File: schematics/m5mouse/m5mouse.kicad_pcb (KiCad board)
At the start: 2 copper layers, 103 x 50 mm, 98 parts, among them IC1 LM3940IMP-3.3_NOPB, J1 Conn_01x02, J2 M-BUS, J3 SWD, J4 Conn_02x03_Odd_Even, J5 Conn_02x03_Odd_Even, J6 Conn_01x03, J7 Conn_01x06, J8 Conn_01x06, Q1 BSS138, Q2 ST-1KL3A, Q3 BSS138, Q4 ST-1KL3A, Q5 BSS138, Q6 ST-1KL3A, Q7 BSS138, Q8 ST-1KL3A, SW1 SW_SPDT, SW2 SW_Push, U1 TPS562200, U2 STM32F405RGTx, U3 DRV8835, U4 ICM-20648, Y1 8MHz, Y2 32.768kHz

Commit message: Fix path
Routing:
- net +3V3: track 203.6 -> 199.1 mm, vias 5 -> 6
- net Net-(C19-Pad1): track 65.8 -> 64.9 mm

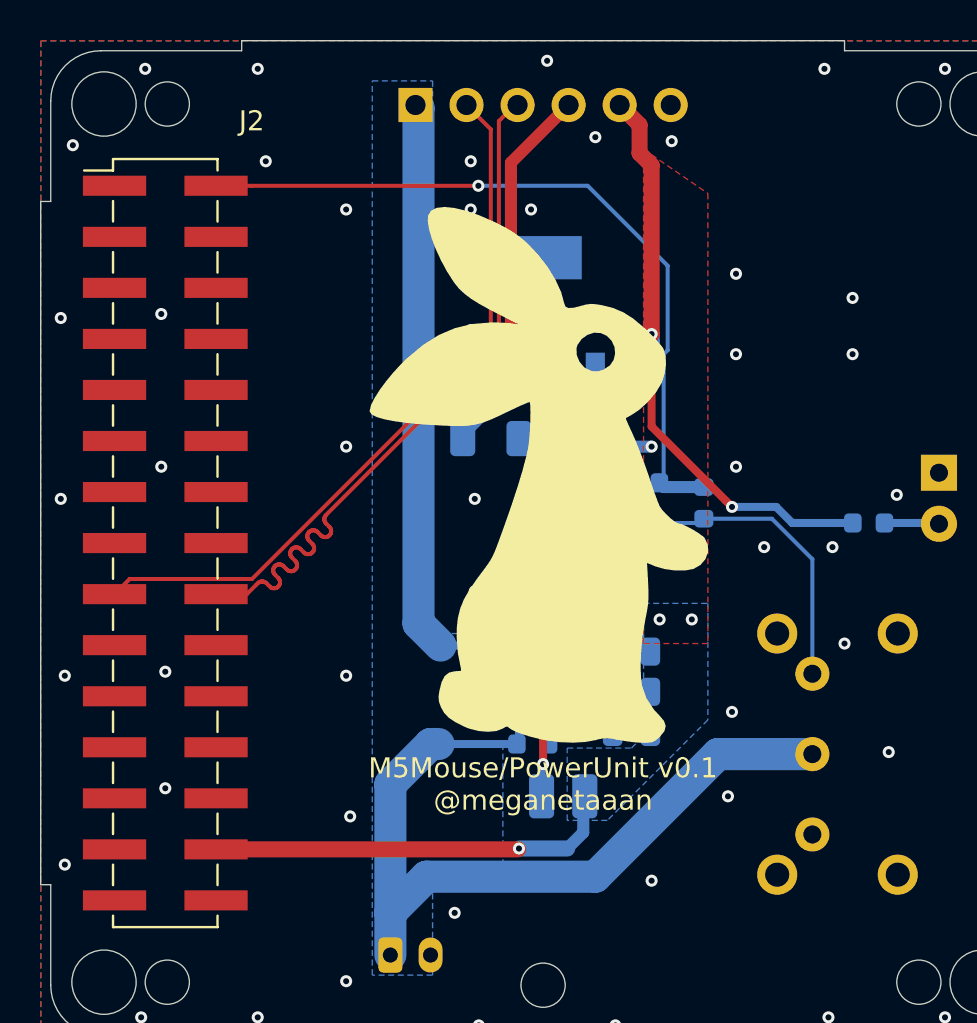
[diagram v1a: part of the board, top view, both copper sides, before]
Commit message: Fix flipped pin header
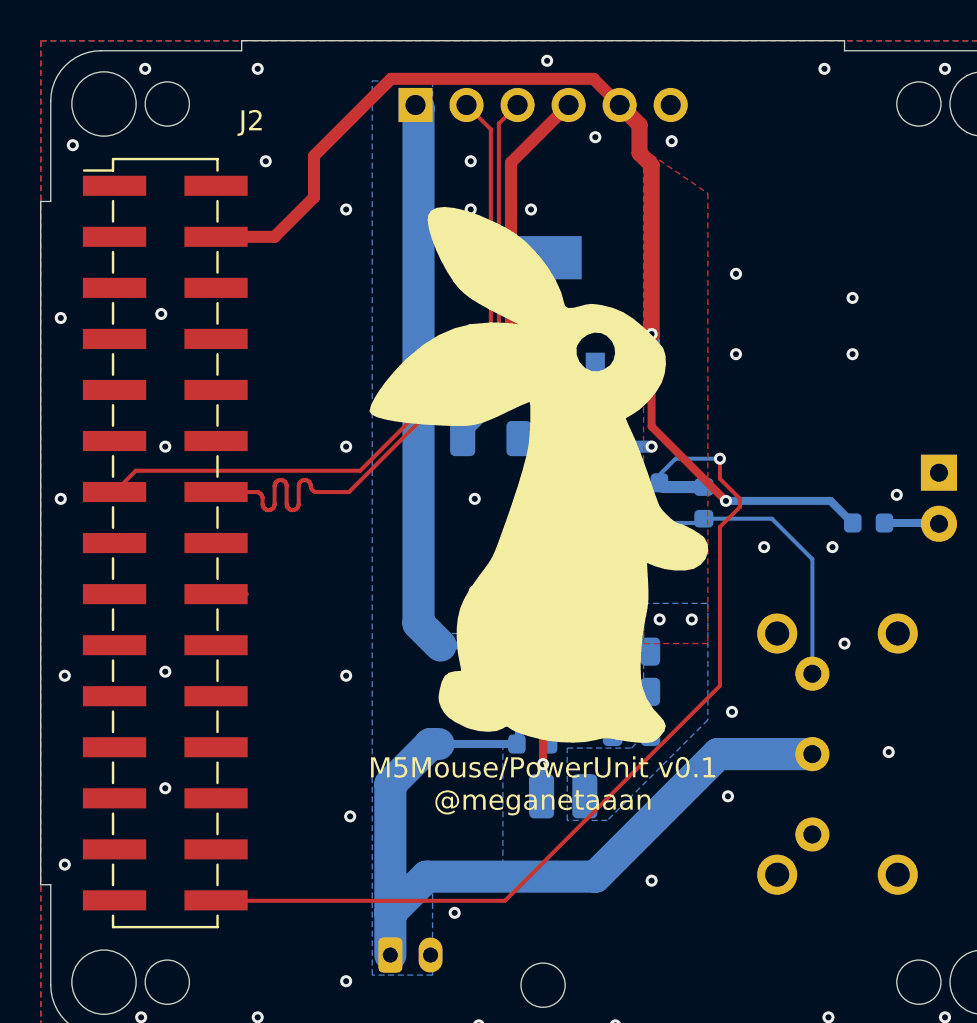
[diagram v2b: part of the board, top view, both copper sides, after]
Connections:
- J2 pad 1: GND -> Net-(J2-Pad1)
- J2 pad 13: Net-(J2-Pad13) -> M5_I2C1_SDA
- J2 pad 14: Net-(J2-Pad14) -> M5_I2C1_SCL
- J2 pad 17: M5_I2C1_SDA -> Net-(J2-Pad17)
- J2 pad 18: M5_I2C1_SCL -> Net-(J2-Pad18)
- J2 pad 2: ADC_BAT -> Net-(J2-Pad2)
- J2 pad 25: Net-(J2-Pad25) -> GND
- J2 pad 27: Net-(J2-Pad27) -> GND
- J2 pad 28: +5V -> Net-(J2-Pad28)
- J2 pad 29: Net-(J2-Pad29) -> GND
- J2 pad 3: GND -> Net-(J2-Pad3)
- J2 pad 30: Net-(J2-Pad30) -> ADC_BAT
- J2 pad 4: Net-(J2-Pad4) -> +5V
- J2 pad 5: GND -> Net-(J2-Pad5)
- Y2 pad 4: (no net) -> Net-(Y2-Pad4)
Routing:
- net ADC_BAT: track 37.4 -> 47.7 mm
- net +5V: track 110.3 -> 114.9 mm, vias 6 -> 5
- net M5_I2C1_SDA: track 36.2 -> 34.1 mm
- net M5_I2C1_SCL: track 36.2 -> 34.1 mm
- net GND: vias 138 -> 137
